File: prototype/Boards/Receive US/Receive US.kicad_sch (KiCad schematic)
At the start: 36 parts, among them J1 Header, Q1 BC848BLT3G, U1 TLV9052SIDGSR, U2 TLV9052SIDGSR

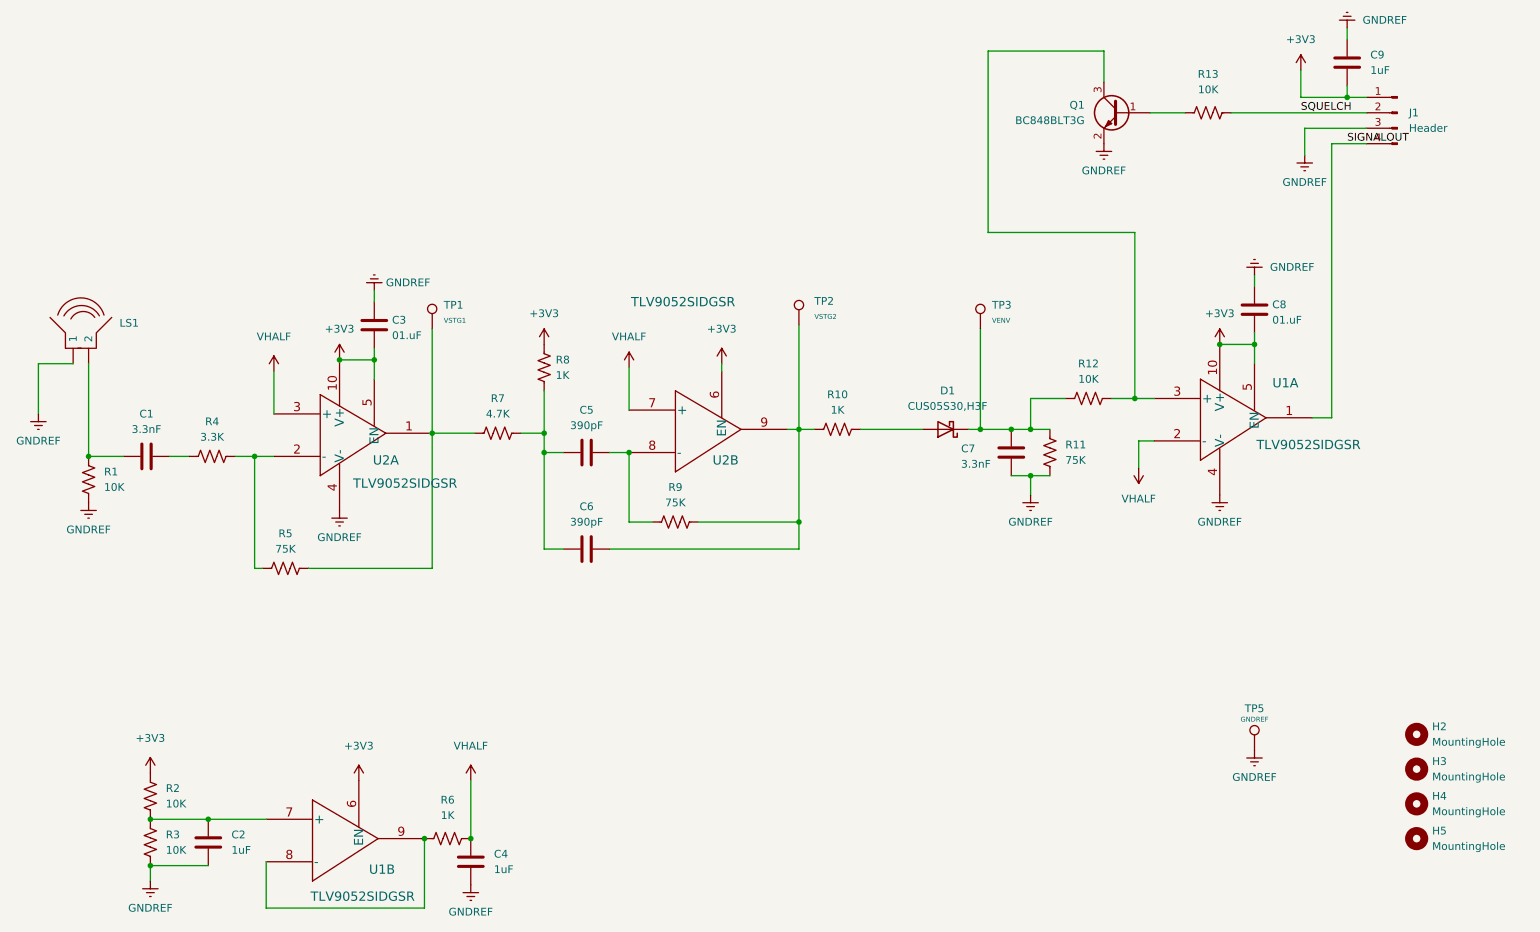
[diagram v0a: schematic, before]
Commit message: Update logo on receiver board; add new logo footprint & symbol
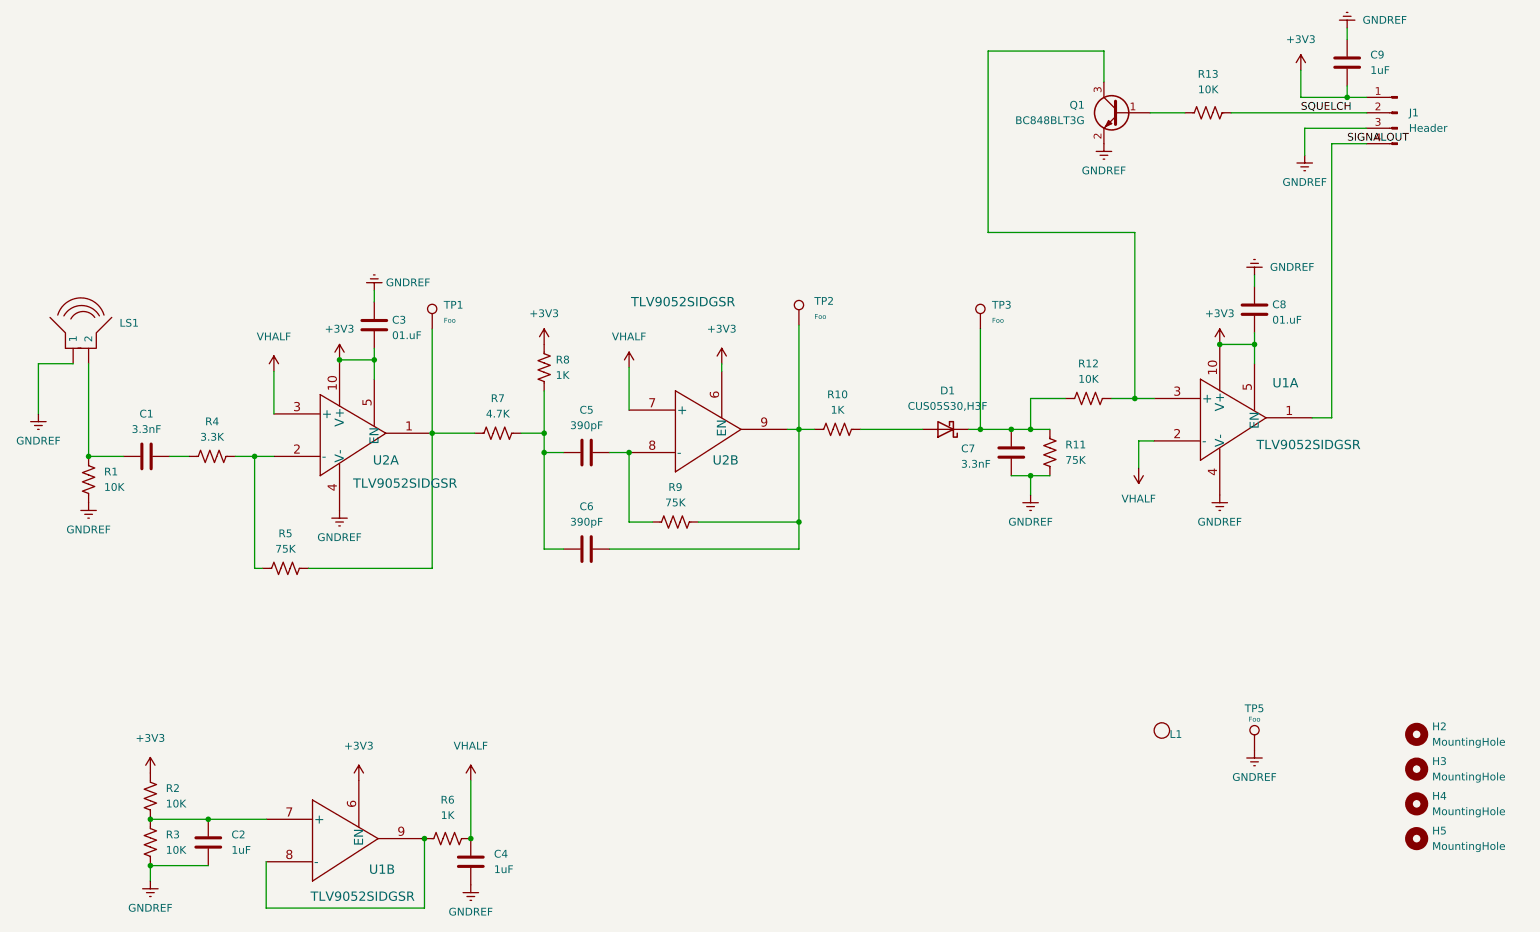
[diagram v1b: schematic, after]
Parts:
- added L1: ~, uFinder:uFollowLogo, symbol uFinder:Logo
- TP1: Net VSTG1 -> Foo
- TP2: Net VSTG2 -> Foo
- TP3: Net VENV -> Foo
- TP5: Net GNDREF -> Foo
